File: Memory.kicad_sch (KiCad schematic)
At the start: 6 parts, among them U7 ESP-PSRAM32

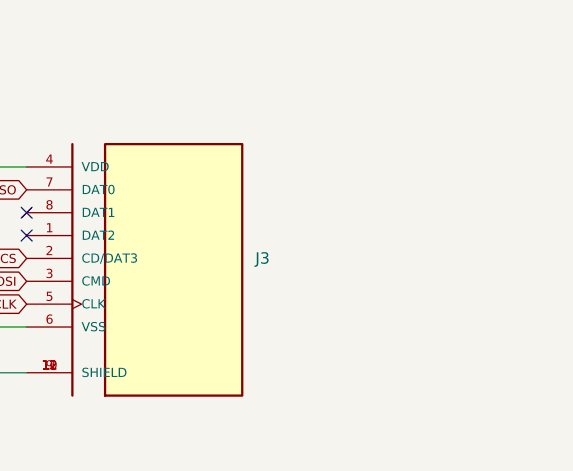
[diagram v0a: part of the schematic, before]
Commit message: added a pinheader for analog signal in
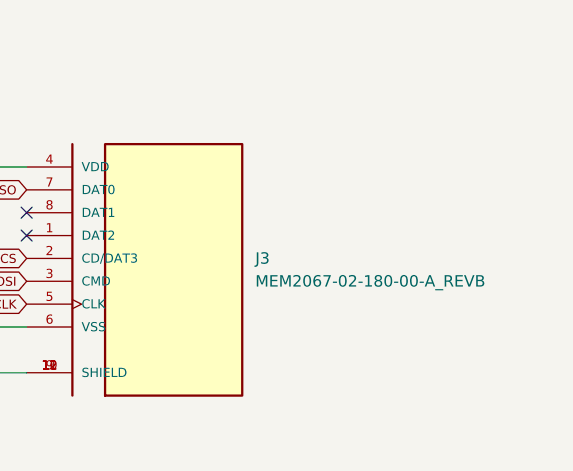
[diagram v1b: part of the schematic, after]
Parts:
- J3: value (none) -> MEM2067-02-180-00-A_REVB; footprint (none) -> SnapEDA Library:GCT_MEM2067-02-180-00-A_REVB
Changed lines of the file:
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@@
       (effects (font (size 1.27 1.27)) (justify left))
     )
-    (property "Value" "" (id 1) (at 219.71 130.8099 0)
+    (property "Value" "MEM2067-02-180-00-A_REVB" (id 1) (at 219.71 130.8099 0)
       (effects (font (size 1.27 1.27)) (justify left))
     )
-    (property "Footprint" "" (id 2) (at 199.39 128.27 0)
+    (property "Footprint" "SnapEDA Library:GCT_MEM2067-02-180-00-A_REVB" (id 2) (at 199.39 128.27 0)
       (effects (font (size 1.27 1.27)) (justify left bottom) hide)
     )

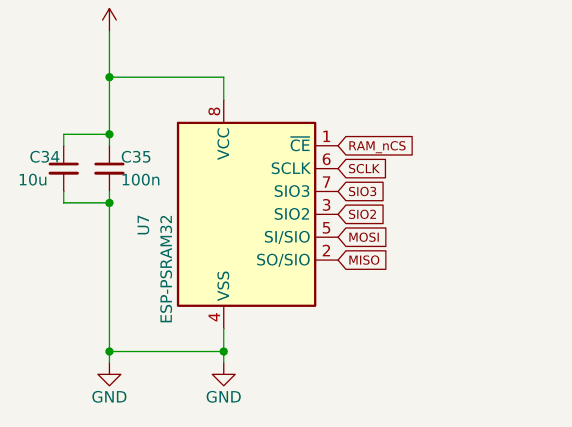
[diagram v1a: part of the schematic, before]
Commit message: added some relevant datasheets
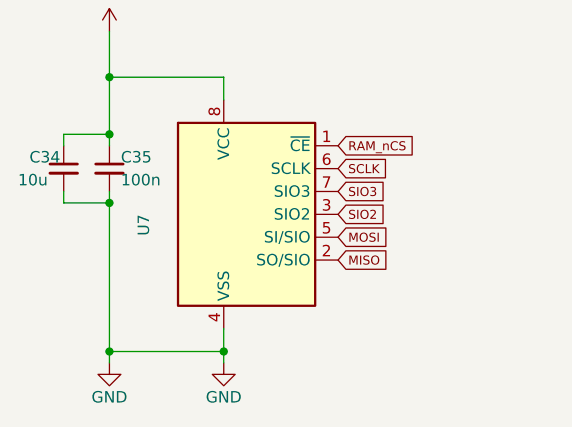
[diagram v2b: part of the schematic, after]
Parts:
- U7: value ESP-PSRAM32 -> (none); footprint Package_SO:SOIC-8_3.9x4.9mm_P1.27mm -> (none)
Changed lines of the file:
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@@
       (effects (font (size 1.27 1.27)) (justify right))
     )
-    (property "Value" "ESP-PSRAM32" (id 1) (at 53.34 128.27 90)
+    (property "Value" "" (id 1) (at 53.34 128.27 90)
       (effects (font (size 1.27 1.27)) (justify right))
     )
-    (property "Footprint" "Package_SO:SOIC-8_3.9x4.9mm_P1.27mm" (id 2) (at 62.23 143.51 0)
+    (property "Footprint" "" (id 2) (at 62.23 143.51 0)
       (effects (font (size 1.27 1.27)) hide)
     )

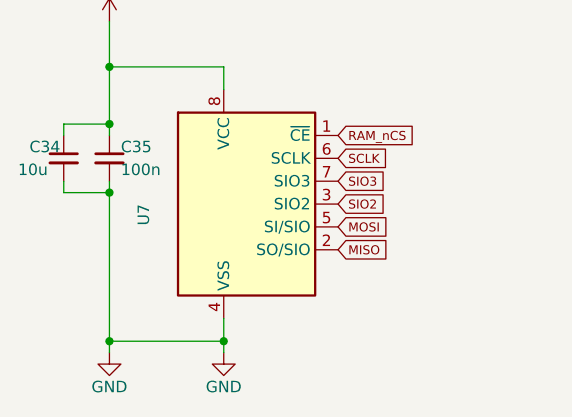
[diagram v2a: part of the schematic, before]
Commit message: changed footprint of caps
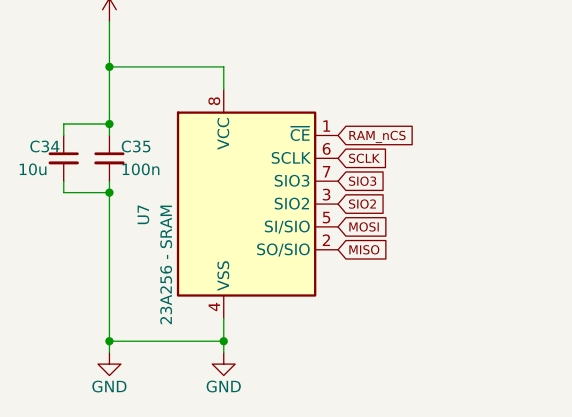
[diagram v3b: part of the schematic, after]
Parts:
- U7: value (none) -> 23A256 - SRAM; footprint (none) -> Package_SO:SOIC-8_3.9x4.9mm_P1.27mm
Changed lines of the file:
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@@
       (effects (font (size 1.27 1.27)) (justify right))
     )
-    (property "Value" "" (id 1) (at 53.34 128.27 90)
+    (property "Value" "23A256 - SRAM" (id 1) (at 53.34 128.27 90)
       (effects (font (size 1.27 1.27)) (justify right))
     )
-    (property "Footprint" "" (id 2) (at 62.23 143.51 0)
+    (property "Footprint" "Package_SO:SOIC-8_3.9x4.9mm_P1.27mm" (id 2) (at 62.23 143.51 0)
       (effects (font (size 1.27 1.27)) hide)
     )

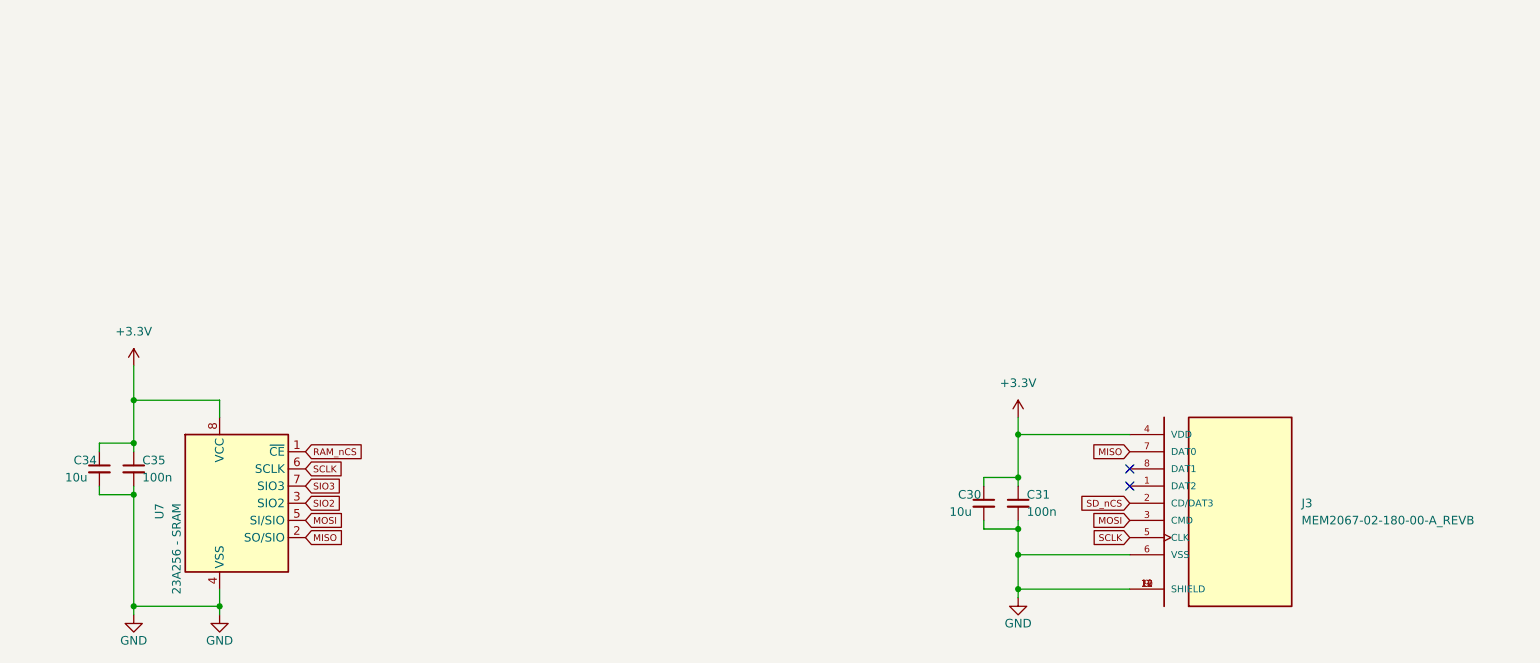
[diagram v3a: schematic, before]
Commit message: grounded mounting holes gnd top layer polygon and cool looking gnd strips on analog side
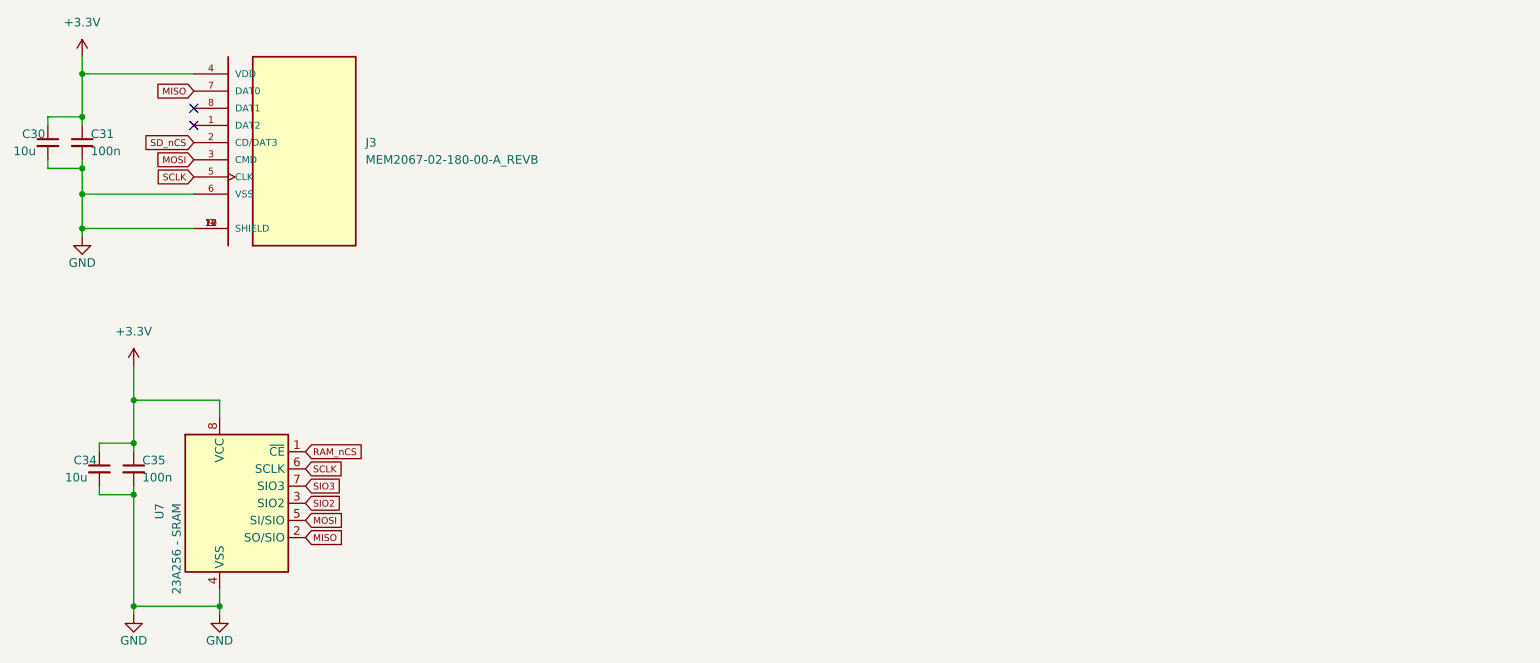
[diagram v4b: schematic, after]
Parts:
- C30, C31, C34, C35: footprint Resistor_SMD:R_0603_1608Metric_Pad0.98x0.95mm_HandSolder -> Capacitor_SMD:C_0603_1608Metric_Pad1.08x0.95mm_HandSolder
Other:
- moved on the sheet: C30, C31, J3

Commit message: smaller pcb removed ram unneccessary
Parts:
- removed C30, C34: 10u, Capacitor_SMD:C_0603_1608Metric_Pad1.08x0.95mm_HandSolder, symbol Device:C_Small
- removed C31, C35: 100n, Capacitor_SMD:C_0603_1608Metric_Pad1.08x0.95mm_HandSolder, symbol Device:C_Small
- removed J3: MEM2067-02-180-00-A_REVB, SnapEDA Library:GCT_MEM2067-02-180-00-A_REVB, symbol MEM2067-02-180-00-A_REVB:MEM2067-02-180-00-A_REVB
- removed U7: 23A256 - SRAM, Package_SO:SOIC-8_3.9x4.9mm_P1.27mm, symbol Memory_RAM:ESP-PSRAM32
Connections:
- no-connect marks 2 -> 0
